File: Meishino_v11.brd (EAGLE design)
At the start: 90.2 x 54.6 mm, 31 parts, among them CN5 CON_AVRISPTH, CN9 CON_USB-BMICRO-B_PCB, Q1 TR_NMOS_2N7000, U1 IC_FT232RQ, U2 MCU_ATMEGA328P_ARDUINO_DIP28, U3 MOD_AE_FT232_DIP24

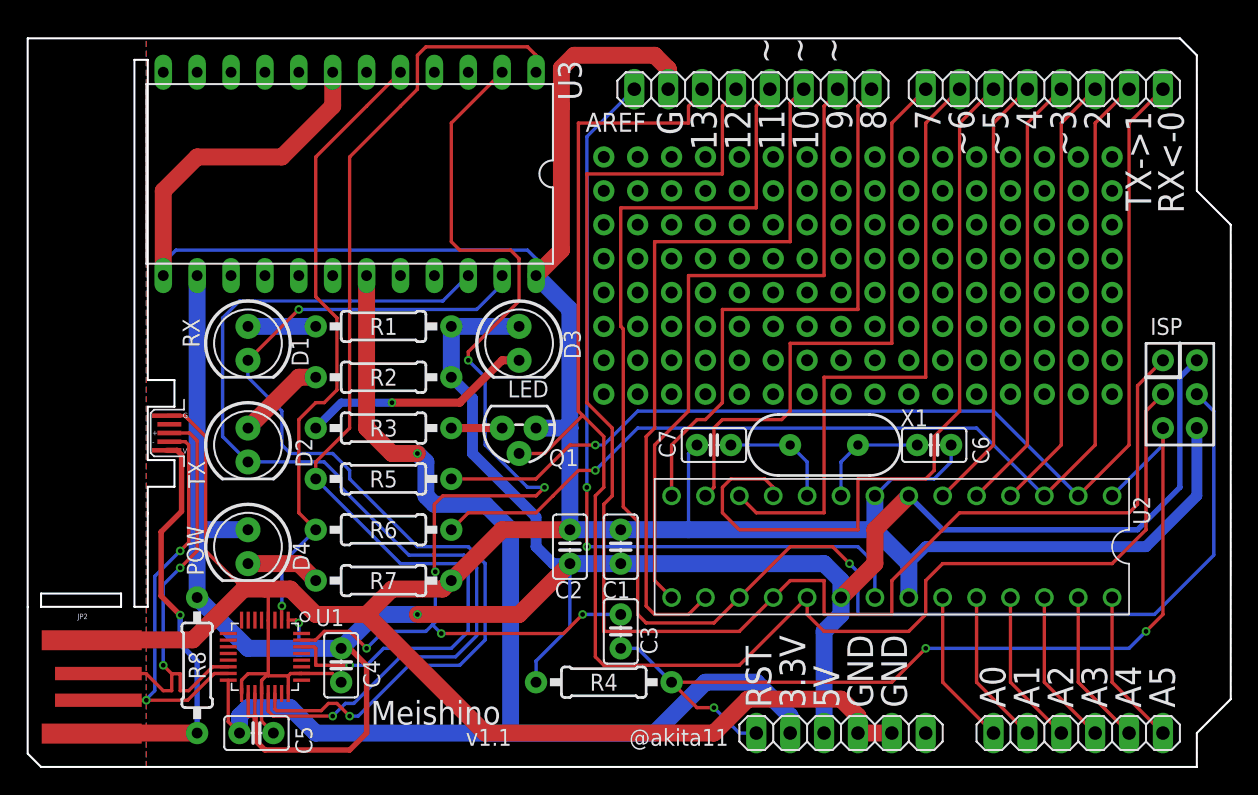
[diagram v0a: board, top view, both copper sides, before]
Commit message: リセットとネジ穴を追加、シルクの調整。
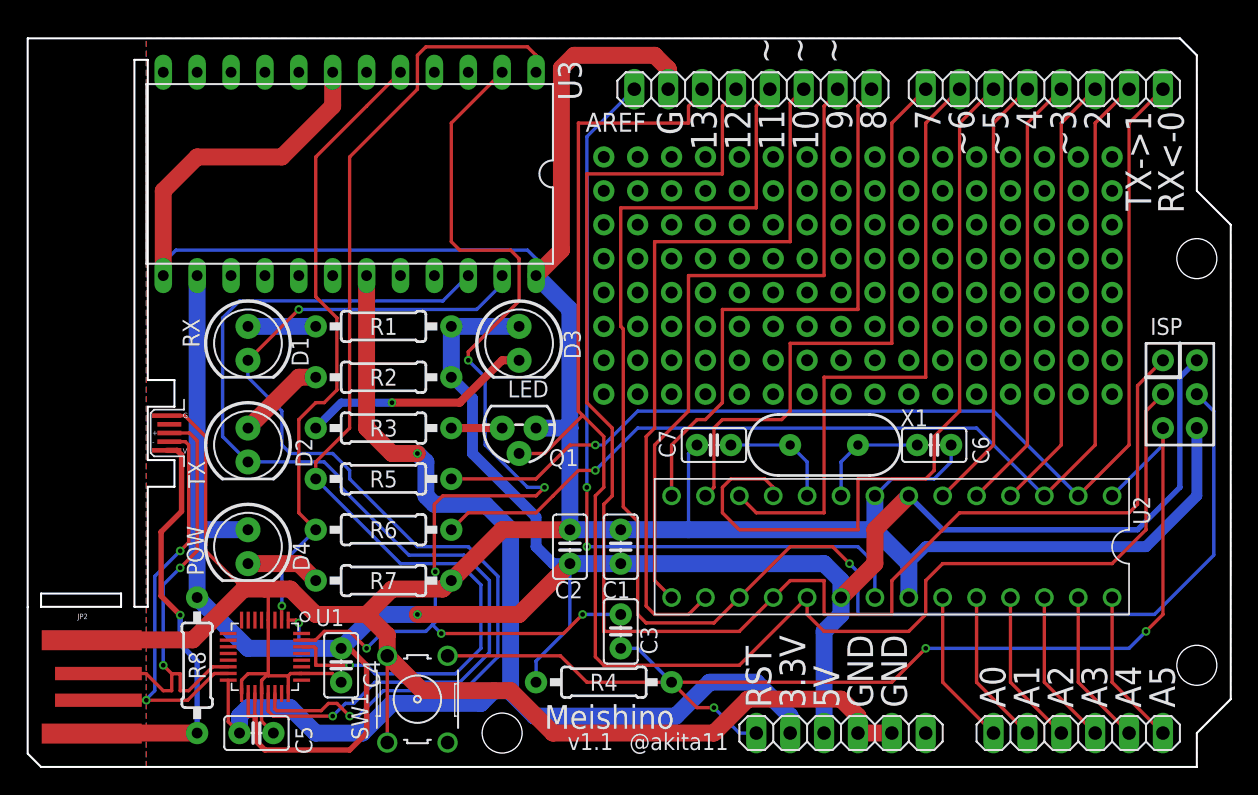
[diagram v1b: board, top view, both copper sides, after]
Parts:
- added SW1: (no value), akita:SW_B3F-10XX
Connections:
- net GND: now also SW1.1, SW1.2
- net RSTN: now also SW1.4
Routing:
- net RSTN: track 72.4 -> 90.0 mm
- net GND: track 306.9 -> 313.9 mm
- net TXD: track 79.2 -> 81.8 mm
- net CB1: track 76.8 -> 78.9 mm
- net CB0: track 74.4 -> 76.5 mm
- net +3V3: track 93.9 -> 92.4 mm
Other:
- outline, holes or cut-outs redrawn

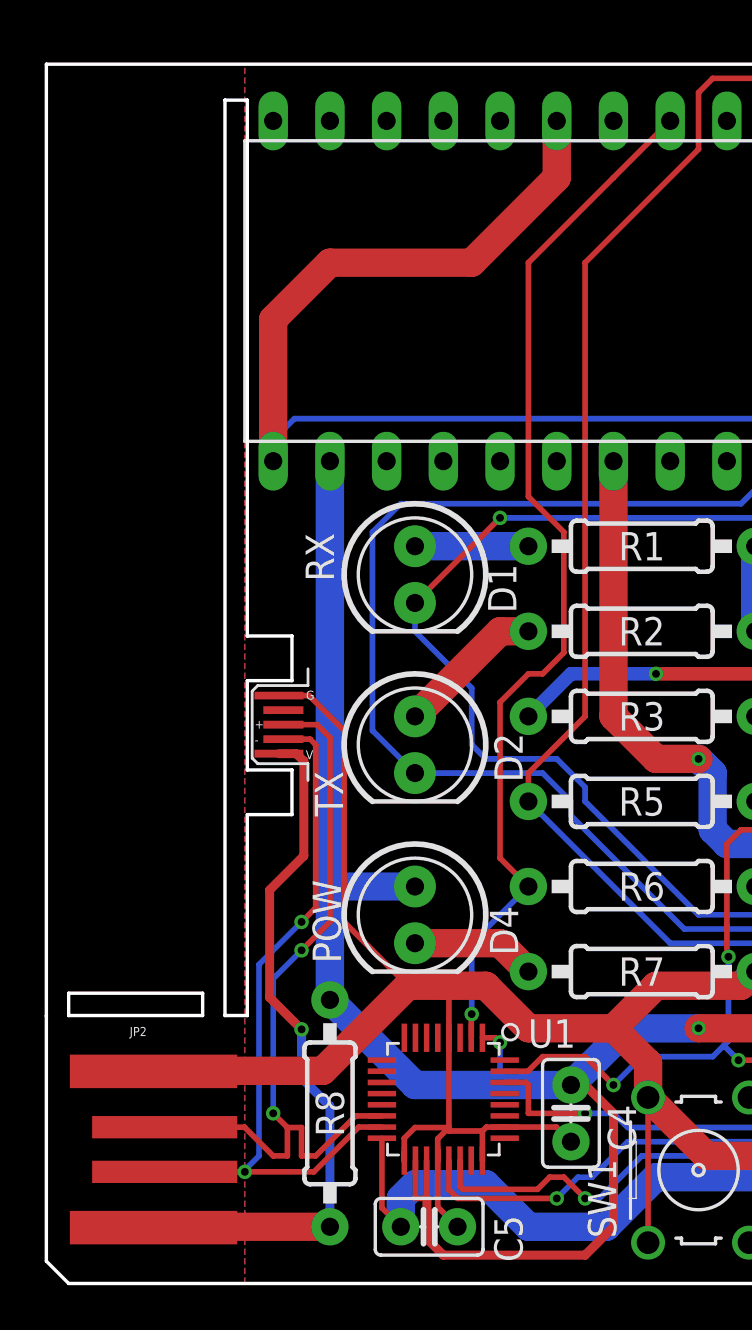
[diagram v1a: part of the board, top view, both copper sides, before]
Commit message: 基板uUSBコネクタの形状を修正
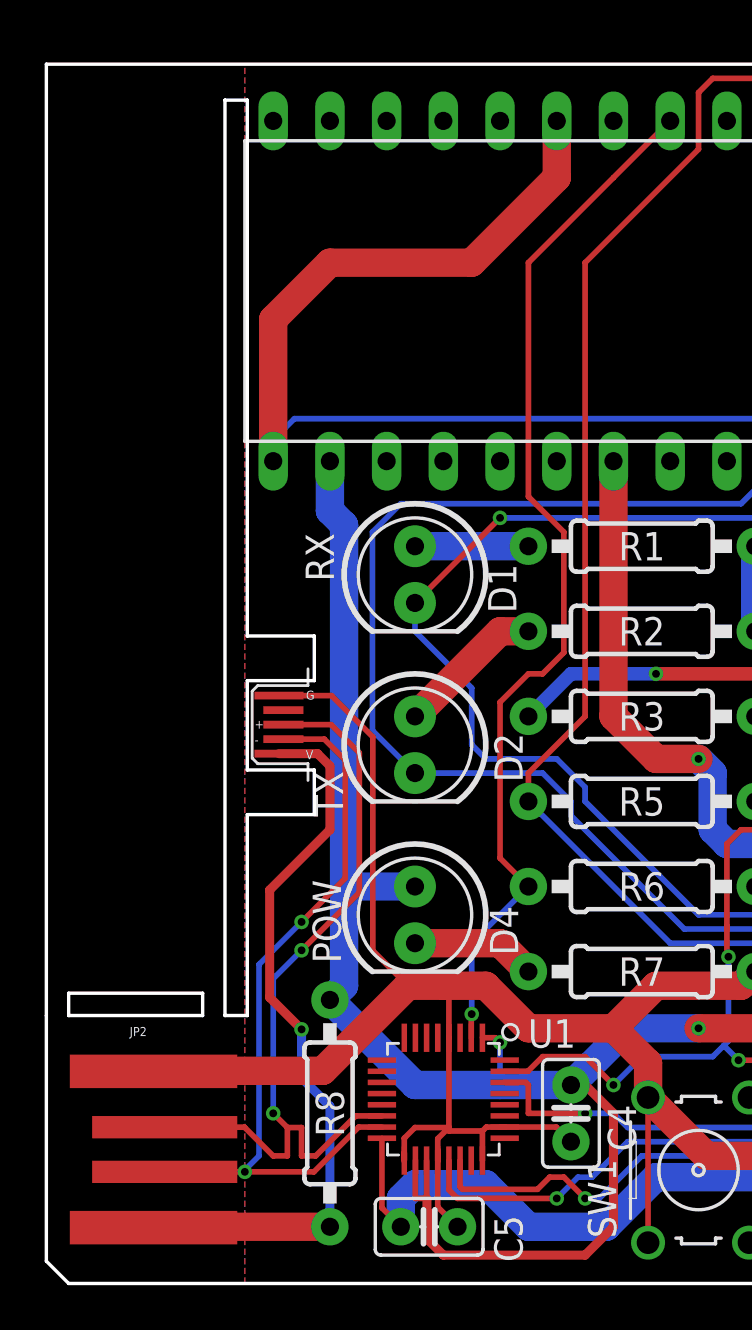
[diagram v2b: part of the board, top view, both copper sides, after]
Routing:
- net N$18: track 31.8 -> 33.3 mm
- net N$9: track 34.6 -> 36.1 mm
- net N$12: track 32.6 -> 34.0 mm
- net GND: track 313.9 -> 314.5 mm
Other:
- outline, holes or cut-outs redrawn
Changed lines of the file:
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@@
 <?xml version="1.0" encoding="utf-8"?>
 <!DOCTYPE eagle SYSTEM "eagle.dtd">
-<eagle version="9.0.1">
+<eagle version="9.1.0">
 <drawing>
 <settings>
@@
 <setting verticaltext="up"/>
 </settings>
-<grid distance="1.27" unitdist="mm" unit="mm" style="lines" multiple="1" display="yes" altdistance="0.3175" altunitdist="mm" altunit="mm"/>
+<grid distance="1" unitdist="mm" unit="mm" style="lines" multiple="1" display="yes" altdistance="0.3175" altunitdist="mm" altunit="mm"/>
 <layers>
 <layer number="1" name="Top" color="4" fill="1" visible="yes" active="yes"/>
@@
 <layer number="17" name="Pads" color="2" fill="1" visible="yes" active="yes"/>
 <layer number="18" name="Vias" color="2" fill="1" visible="yes" active="yes"/>
-<layer number="19" name="Unrouted" color="6" fill="1" visible="no" active="yes"/>
+<layer number="19" name="Unrouted" color="6" fill="1" visible="yes" active="yes"/>
 <layer number="20" name="Dimension" color="24" fill="1" visible="yes" active="yes"/>
 <layer number="21" name="tPlace" color="7" fill="1" visible="yes" active="yes"/>
@@
 <wire x1="87.63" y1="53.34" x2="86.36" y2="54.61" width="0.1524" layer="20"/>
 <wire x1="86.36" y1="54.61" x2="0" y2="54.61" width="0.1524" layer="20"/>
-<wire x1="9" y1="29" x2="11" y2="29" width="0.1524" layer="20"/>
-<wire x1="11" y1="29" x2="11" y2="27" width="0.1524" layer="20"/>
-<wire x1="11" y1="27" x2="9" y2="27" width="0.1524" layer="20"/>
+<wire x1="9" y1="29" x2="12" y2="29" width="0.1524" layer="20"/>
+<wire x1="12" y1="29" x2="12" y2="27" width="0.1524" layer="20"/>
+<wire x1="12" y1="27" x2="9" y2="27" width="0.1524" layer="20"/>
 <wire x1="9" y1="27" x2="9" y2="23" width="0.1524" layer="20"/>
-<wire x1="9" y1="23" x2="11" y2="23" width="0.1524" layer="20"/>
-<wire x1="11" y1="23" x2="11" y2="21" width="0.1524" layer="20"/>
-<wire x1="11" y1="21" x2="9" y2="21" width="0.1524" layer="20"/>
+<wire x1="9" y1="23" x2="12" y2="23" width="0.1524" layer="20"/>
+<wire x1="12" y1="23" x2="12" y2="21" width="0.1524" layer="20"/>
+<wire x1="12" y1="21" x2="9" y2="21" width="0.1524" layer="20"/>
 <wire x1="0" y1="12" x2="0" y2="1" width="0.1524" layer="20"/>
 <wire x1="0" y1="1" x2="1" y2="0" width="0.1524" layer="20"/>
@@
 <rectangle x1="1.1875" y1="11.7275" x2="13.0275" y2="11.8075" layer="22"/>
 <rectangle x1="1.1875" y1="11.8075" x2="13.0275" y2="11.8875" layer="22"/>
-<wire x1="0" y1="11.97" x2="0" y2="54.61" width="0.1524" layer="20"/>
+<wire x1="0" y1="12" x2="0" y2="54.61" width="0.1524" layer="20"/>
 <wire x1="9" y1="53" x2="9" y2="29" width="0.1524" layer="20"/>
 <wire x1="9" y1="21" x2="9" y2="12" width="0.1524" layer="20"/>
@@
 <param name="checkStop" value="0"/>
 <param name="checkValues" value="0"/>
+<param name="checkNames" value="1"/>
+<param name="checkWireStubs" value="1"/>
+<param name="checkPolygonWidth" value="0"/>
 <param name="useDiameter" value="13"/>
 <param name="maxErrors" value="50"/>
@@
 <wire x1="40.64" y1="17.78" x2="35.56" y2="17.78" width="1.27" layer="1"/>
 <wire x1="35.56" y1="17.78" x2="31.75" y2="13.97" width="1.27" layer="1"/>
-<wire x1="11.77" y1="26.33" x2="13.335" y2="24.765" width="0.254" layer="1"/>
-<wire x1="13.335" y1="24.765" x2="13.335" y2="16.1925" width="0.254" layer="1"/>
-<wire x1="13.335" y1="16.1925" x2="16.1925" y2="13.335" width="0.254" layer="1"/>
-<wire x1="10.4175" y1="26.33" x2="11.77" y2="26.33" width="0.254" layer="1"/>
+<wire x1="12.77" y1="26.33" x2="14.6225" y2="24.4775" width="0.254" layer="1"/>
+<wire x1="14.6225" y1="24.4775" x2="14.6225" y2="14.905" width="0.254" layer="1"/>
+<wire x1="14.6225" y1="14.905" x2="16.1925" y2="13.335" width="0.254" layer="1"/>
+<wire x1="10.4175" y1="26.33" x2="12.77" y2="26.33" width="0.254" layer="1"/>
 <wire x1="27.305" y1="13.335" x2="31.115" y2="13.335" width="1.27" layer="1"/>
 <wire x1="31.115" y1="13.335" x2="31.75" y2="13.97" width="1.27" layer="1"/>
@@
 <wire x1="59.69" y1="15.24" x2="60.96" y2="13.97" width="1.27" layer="16"/>
 <wire x1="60.96" y1="13.97" x2="60.96" y2="12.7" width="1.27" layer="16"/>
-<wire x1="12.7" y1="36.83" x2="12.7" y2="19.05" width="1.27" layer="16"/>
-<wire x1="12.7" y1="19.05" x2="12.7" y2="17.78" width="1.27" layer="16"/>
-<wire x1="12.7" y1="17.78" x2="12.7" y2="12.7" width="1.27" layer="16"/>
-<wire x1="16.51" y1="17.78" x2="12.7" y2="17.78" width="1.27" layer="16"/>
 <wire x1="17.03" y1="5.505" x2="17.03" y2="3.81" width="0.254" layer="1"/>
 <wire x1="16.53" y1="5.505" x2="16.53" y2="3.81" width="0.254" layer="1"/>
@@
 <wire x1="24.13" y1="1.27" x2="17.78" y2="1.27" width="0.4064" layer="1"/>
 <wire x1="24.13" y1="1.27" x2="25.4" y2="2.54" width="0.4064" layer="1"/>
-<wire x1="25.4" y1="2.54" x2="25.4" y2="4.445" width="0.4064" layer="1"/>
-<wire x1="25.4" y1="4.445" x2="25.4" y2="7.62" width="0.4064" layer="1"/>
+<wire x1="25.4" y1="2.54" x2="25.4" y2="7.62" width="0.4064" layer="1"/>
 <wire x1="25.4" y1="7.62" x2="24.13" y2="8.89" width="0.4064" layer="1"/>
 <wire x1="24.13" y1="8.89" x2="23.495" y2="8.89" width="0.4064" layer="1"/>
@@
 <wire x1="36.83" y1="33.02" x2="31.75" y2="33.02" width="1.27" layer="16"/>
 <wire x1="31.75" y1="33.02" x2="31.75" y2="29.21" width="1.27" layer="16"/>
+<wire x1="12.7" y1="36.83" x2="12.7" y2="34.6075" width="1.27" layer="16"/>
+<wire x1="12.7" y1="34.6075" x2="13.335" y2="33.9725" width="1.27" layer="16"/>
+<wire x1="13.335" y1="33.9725" x2="13.335" y2="17.78" width="1.27" layer="16"/>
+<wire x1="13.335" y1="17.78" x2="13.335" y2="13.335" width="1.27" layer="16"/>
+<wire x1="13.335" y1="13.335" x2="12.7" y2="12.7" width="1.27" layer="16"/>
+<wire x1="16.51" y1="17.78" x2="13.335" y2="17.78" width="1.27" layer="16"/>
 </signal>
 <signal name="+3V3">
@@
 <wire x1="4.8" y1="2.5" x2="4.84" y2="2.54" width="1.27" layer="1"/>
 <wire x1="4.84" y1="2.54" x2="12.7" y2="2.54" width="1.27" layer="1"/>
-<wire x1="10.4175" y1="23.73" x2="11.195" y2="23.73" width="0.4064" layer="1"/>
-<wire x1="11.195" y1="23.73" x2="11.5334" y2="23.3916" width="0.4064" layer="1"/>
-<wire x1="11.5334" y1="23.3916" x2="11.5334" y2="19.1534" width="0.4064" layer="1"/>
-<wire x1="11.5334" y1="19.1534" x2="10" y2="17.62" width="0.4064" layer="1"/>
 <wire x1="10" y1="17.62" x2="10" y2="12.8125" width="0.4064" layer="1"/>
 <via x="11.43" y="11.3825" extent="1-16" drill="0.35"/>
@@
 <wire x1="12.7" y1="7.9375" x2="12.7" y2="2.54" width="0.4064" layer="16"/>
 <wire x1="10" y1="12.8125" x2="11.43" y2="11.3825" width="0.4064" layer="1"/>
+<wire x1="10.4175" y1="23.73" x2="12.1475" y2="23.73" width="0.4064" layer="1"/>
+<wire x1="12.1475" y1="23.73" x2="12.7" y2="23.1775" width="0.4064" layer="1"/>
+<wire x1="12.7" y1="23.1775" x2="12.7" y2="20.32" width="0.4064" layer="1"/>
+<wire x1="12.7" y1="20.32" x2="10" y2="17.62" width="0.4064" layer="1"/>
 </signal>
 <signal name="N$14">
@@
 <wire x1="11.43" y1="6.985" x2="10.795" y2="6.985" width="0.254" layer="1"/>
 <wire x1="11.43" y1="5.715" x2="11.43" y2="6.985" width="0.254" layer="1"/>
-<wire x1="12.1175" y1="25.03" x2="12.7" y2="24.4475" width="0.254" layer="1"/>
-<wire x1="12.7" y1="24.4475" x2="12.7" y2="16.1925" width="0.254" layer="1"/>
-<wire x1="12.7" y1="16.1925" x2="11.43" y2="14.9225" width="0.254" layer="1"/>
+<wire x1="12.7525" y1="25.03" x2="14.0175" y2="23.765" width="0.254" layer="1"/>
+<wire x1="14.0175" y1="23.765" x2="14.0175" y2="17.51" width="0.254" layer="1"/>
+<wire x1="14.0175" y1="17.51" x2="11.43" y2="14.9225" width="0.254" layer="1"/>
 <via x="11.43" y="14.9225" extent="1-16" drill="0.35"/>
 <wire x1="11.43" y1="14.9225" x2="10.16" y2="13.6525" width="0.254" layer="16"/>
@@
 <wire x1="10.16" y1="7.62" x2="10.795" y2="6.985" width="0.254" layer="1"/>
 <wire x1="10.16" y1="13.6525" x2="10.16" y2="7.62" width="0.254" layer="16"/>
-<wire x1="10.6175" y1="25.03" x2="12.1175" y2="25.03" width="0.254" layer="1"/>
+<wire x1="10.6175" y1="25.03" x2="12.7525" y2="25.03" width="0.254" layer="1"/>
 </signal>
 <signal name="N$12">
@@
 <wire x1="8.89" y1="5" x2="5.3" y2="5" width="0.254" layer="1"/>
 <wire x1="13.99" y1="7.005" x2="11.985" y2="5" width="0.254" layer="1"/>
-<wire x1="11.815" y1="24.38" x2="12.065" y2="24.13" width="0.254" layer="1"/>
-<wire x1="12.065" y1="16.8275" x2="11.43" y2="16.1925" width="0.254" layer="1"/>
+<wire x1="12.45" y1="24.38" x2="13.3825" y2="23.4475" width="0.254" layer="1"/>
+<wire x1="13.3825" y1="18.145" x2="11.43" y2="16.1925" width="0.254" layer="1"/>
 <via x="11.43" y="16.1925" extent="1-16" drill="0.35"/>
 <wire x1="11.43" y1="16.1925" x2="9.525" y2="14.2875" width="0.254" layer="16"/>
-<wire x1="12.065" y1="24.13" x2="12.065" y2="16.8275" width="0.254" layer="1"/>
+<wire x1="13.3825" y1="23.4475" x2="13.3825" y2="18.145" width="0.254" layer="1"/>
 <wire x1="9.525" y1="14.2875" x2="9.525" y2="5.715" width="0.254" layer="16"/>
 <wire x1="9.525" y1="5.715" x2="8.89" y2="5.08" width="0.254" layer="16"/>
 <wire x1="8.89" y1="5.08" x2="8.89" y2="5" width="0.254" layer="16"/>
 <via x="8.89" y="5" extent="1-16" drill="0.35"/>
-<wire x1="10.6175" y1="24.38" x2="11.815" y2="24.38" width="0.254" layer="1"/>
+<wire x1="10.6175" y1="24.38" x2="12.45" y2="24.38" width="0.254" layer="1"/>
 </signal>
 <signal name="N$19">
@@
 </signal>
 </signals>
+<mfgpreviewcolors>
+<mfgpreviewcolor name="soldermaskcolor" color="0xC8008000"/>
+<mfgpreviewcolor name="silkscreencolor" color="0xFFFEFEFE"/>
+<mfgpreviewcolor name="backgroundcolor" color="0xFF282828"/>
+<mfgpreviewcolor name="coppercolor" color="0xFFFFBF00"/>
+<mfgpreviewcolor name="substratecolor" color="0xFF786E46"/>
+</mfgpreviewcolors>
 </board>
 </drawing>
